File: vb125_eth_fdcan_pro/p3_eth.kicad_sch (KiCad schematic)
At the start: 43 parts, among them J4 ARJM11C7-114-BA-EW2, U2 LAN8740A, X2 50MHz

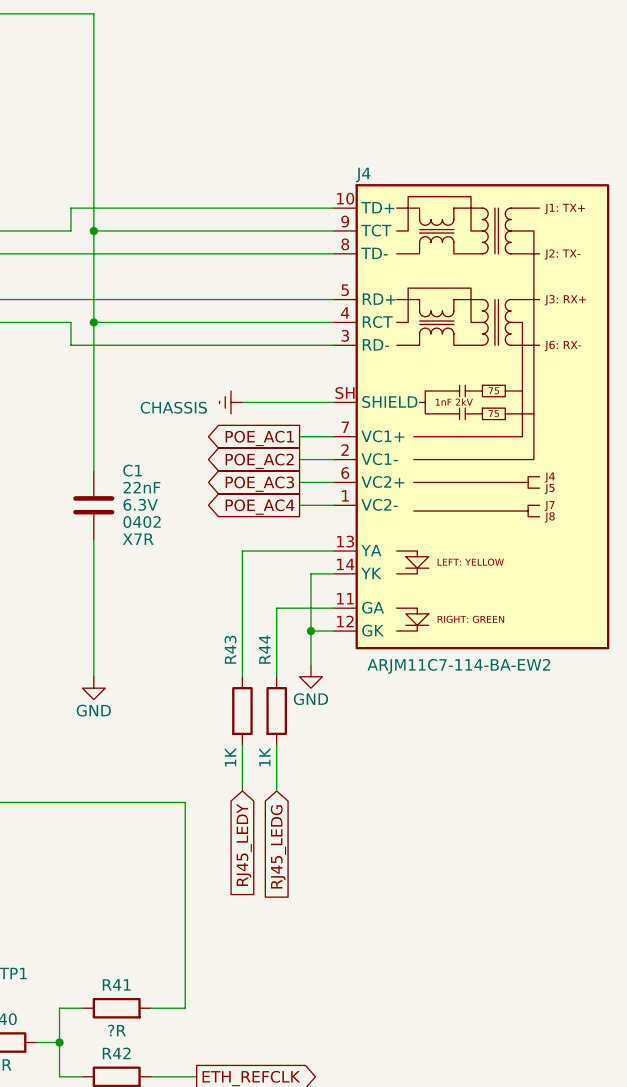
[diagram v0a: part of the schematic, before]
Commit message: Preliminary placement.
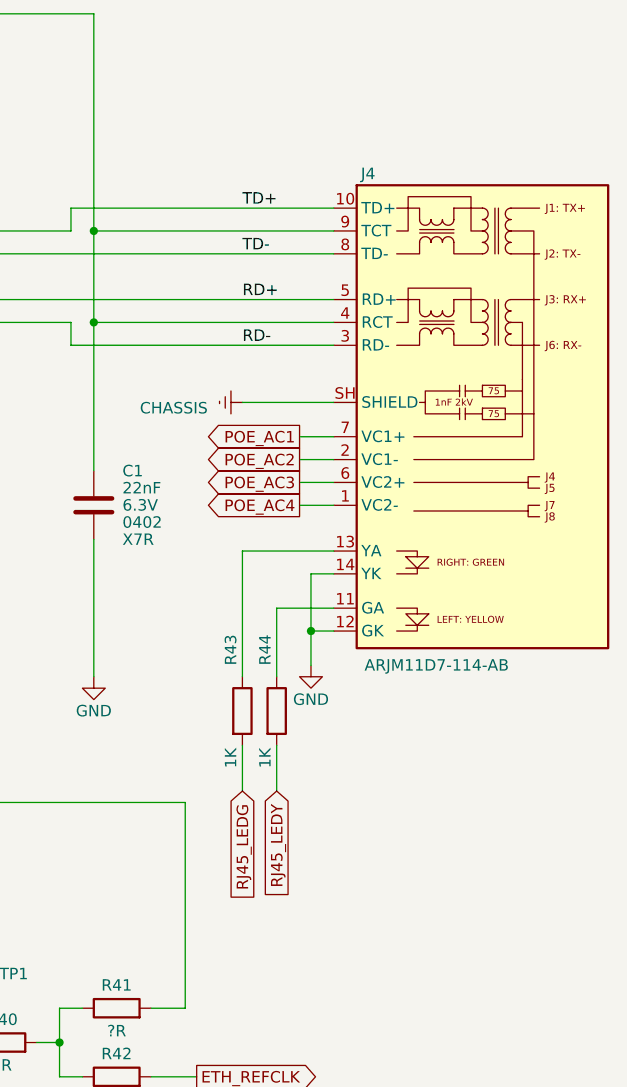
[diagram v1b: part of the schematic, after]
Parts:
- removed J4: ARJM11C7-114-BA-EW2, vhrd_connector_abracon:RJ45_Abracon_ARJM11_7POE_LED, symbol vhrd_connector_abracon:ARJM11C7-114-BA
- added J4: ARJM11D7-114-AB, vhrd_connector_abracon:ARJM11D7-114-AB-EW2, symbol vhrd_connector_abracon:ARJM11D7-114-AB
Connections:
- net +AVDD_PHY: now also J4.4 (RCT), J4.9 (TCT)
- net CHASSIS: now also J4.SH (SHIELD)
- net GND: now also J4.12 (GK), J4.14 (YK)
- net POE_AC1: now also J4.7 (VC1+)
- net POE_AC2: now also J4.2 (VC1-)
- net POE_AC3: now also J4.6 (VC2+)
- net POE_AC4: now also J4.1 (VC2-)
- net RJ45_LEDG: now also R43.2; no longer R44.2
- net RJ45_LEDY: now also R44.2; no longer R43.2
- net RD-: now reaches D1.1 (I/O_1), R35.2, U2.30 (RXN)
- net RD-: now also J4.3 (RD-)
- net TD-: now reaches D1.3 (I/O_2), R38.2, U2.28 (TXN)
- net TD-: now also J4.8 (TD-)
- net at R43.1: now also J4.13 (YA)
- net TD+: now reaches D1.4 (I/O_3), R39.2, U2.29 (TXP)
- net TD+: now also J4.10 (TD+)
- net RD+: now reaches D1.6 (I/O_4), R36.2, U2.31 (RXP)
- net RD+: now also J4.5 (RD+)
- net at R44.1: now also J4.11 (GA)
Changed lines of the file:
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@@
+    (effects (font (size 1.27 1.27)) (justify left bottom))
+  )
+  (label "RD+" (at 302.26 90.17 0) (fields_autoplaced)
     (effects (font (size 1.27 1.27)) (justify left bottom))
   )
@@
     (effects (font (size 1.27 1.27)) (justify left bottom))
   )
+  (label "TD+" (at 302.26 80.01 0) (fields_autoplaced)
+    (effects (font (size 1.27 1.27)) (justify left bottom))
+  )
   (label "PHYAD1" (at 168.91 128.27 0) (fields_autoplaced)
     (effects (font (size 1.27 1.27)) (justify left bottom))
   )
+  (label "TD-" (at 302.26 85.09 0) (fields_autoplaced)
+    (effects (font (size 1.27 1.27)) (justify left bottom))
+  )
   (label "RBIAS" (at 154.94 196.85 0) (fields_autoplaced)
     (effects (font (size 1.27 1.27)) (justify left bottom))
   )
   (label "RXD2_NU" (at 165.1 120.65 0) (fields_autoplaced)
+    (effects (font (size 1.27 1.27)) (justify left bottom))
+  )
+  (label "RD-" (at 302.26 95.25 0) (fields_autoplaced)
     (effects (font (size 1.27 1.27)) (justify left bottom))
   )
@@
     )
   )
-  (global_label "RJ45_LEDG" (shape input) (at 306.07 144.78 270) (fields_autoplaced)
+  (global_label "RJ45_LEDG" (shape input) (at 302.26 144.78 270) (fields_autoplaced)
     (effects (font (size 1.27 1.27)) (justify right))
-    (property "Intersheetrefs" "${INTERSHEET_REFS}" (at 306.07 158.0271 90)
+    (property "Intersheetrefs" "${INTERSHEET_REFS}" (at 302.26 158.0271 90)
       (effects (font (size 1.27 1.27)) (justify right) hide)
     )
   )
-  (global_label "RJ45_LEDY" (shape input) (at 302.26 144.78 270) (fields_autoplaced)
+  (global_label "RJ45_LEDY" (shape input) (at 306.07 144.78 270) (fields_autoplaced)
     (effects (font (size 1.27 1.27)) (justify right))
-    (property "Intersheetrefs" "${INTERSHEET_REFS}" (at 302.26 157.8457 90)
+    (property "Intersheetrefs" "${INTERSHEET_REFS}" (at 306.07 157.8457 90)
       (effects (font (size 1.27 1.27)) (justify right) hide)
     )
@@
     )
   )
+  (symbol (lib_id "vhrd_connector_abracon:ARJM11D7-114-AB") (at 314.96 77.47 0) (unit 1)
+    (in_bom yes) (on_board yes) (dnp no)
+    (property "Reference" "J4" (at 316.23 76.2 0)
+      (effects (font (size 1.27 1.27)))
+    )
+    (property "Value" "ARJM11D7-114-AB" (at 323.85 130.81 0)
+      (effects (font (size 1.27 1.27)))
+    )
+    (property "Footprint" "vhrd_connector_abracon:ARJM11D7-114-AB-EW2" (at 330.835 131.445 0)
+      (effects (font (size 1.27 1.27)) hide)
+    )
+    (property "Datasheet" "https://abracon.com/Magnetics/ARJM11.pdf" (at 324.485 133.35 0)
+      (effects (font (size 1.27 1.27)) hide)
+    )
+    (property "Description" "100Mbps integrated magnetics and PoE 350mA (cont)" (at 370.84 106.3625 0)
+      (effects (font (size 1.27 1.27)) hide)
+    )
+    (pin "1")
+    (pin "10")
+    (pin "11")
+    (pin "12")
+    (pin "13")
+    (pin "14")
+    (pin "2")
+    (pin "3")
+    (pin "4")
+    (pin "5")
+    (pin "6")
+    (pin "7")
+    (pin "8")
+    (pin "9")
+    (pin "SH")
+    (instances
+      (project "vb125_eth_fdcan_pro"
+        (path "/b473bccb-f14c-41d5-b473-137d3ef8ae1e/6eaf8f36-f4c1-413f-846c-b502b7be2b8c"
+          (reference "J4") (unit 1)
+        )
+      )
+    )
+  )
   (symbol (lib_id "Connector:TestPoint_Probe") (at 270.51 187.96 0) (unit 1)
     (in_bom yes) (on_board yes) (dnp no)
@@
         )
       )
-    )
-  )
-  (symbol (lib_id "vhrd_connector_abracon:ARJM11C7-114-BA") (at 314.96 77.47 0) (unit 1)
-    (in_bom yes) (on_board yes) (dnp no)
-    (property "Reference" "J4" (at 314.96 76.2 0)
-      (effects (font (size 1.27 1.27)) (justify left))
-    )
-    (property "Value" "ARJM11C7-114-BA-EW2" (at 326.39 130.81 0)
-      (effects (font (size 1.27 1.27)))
-    )
-    (property "Footprint" "vhrd_connector_abracon:RJ45_Abracon_ARJM11_7POE_LED" (at 327.66 101.6 0)
-      (effects (font (size 1.27 1.27)) hide)
-    )
-    (property "Datasheet" "https://abracon.com/Magnetics/ARJM11.pdf" (at 327.66 101.6 0)
-      (effects (font (size 1.27 1.27)) hide)
-    )
-    (property "Description" "100Mbps integrated magnetics and PoE 350mA (cont)" (at 329.565 135.255 0)
-      (effects (font (size 1.27 1.27)) hide)
-    )
-    (pin "1")
-    (pin "10")
-    (pin "11")
-    (pin "12")
-    (pin "13")
-    (pin "14")
-    (pin "2")
-    (pin "3")
-    (pin "4")
-    (pin "5")
-    (pin "6")
-    (pin "7")
-    (pin "8")
-    (pin "9")
-    (pin "SH")
-    (instances
-      (project "vb125_eth_fdcan_pro"
-        (path "/b473bccb-f14c-41d5-b473-137d3ef8ae1e/6eaf8f36-f4c1-413f-846c-b502b7be2b8c"
-          (reference "J4") (unit 1)
-        )
-      )

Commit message: Finish layout.
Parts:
- removed C1: 100nF, Capacitor_SMD:C_0402_1005Metric, symbol Device:C
- removed D1: D5V0P4UR6SO-7, vhrd_passive_tvs:D5V0P4UR6SO-7, symbol vhrd_passive_tvs:D5V0P4UR6SO-7
- added D16 (x2): RCLAMP0502BA, Package_TO_SOT_SMD:SOT-416, symbol Power_Protection:RCLAMP0502BA
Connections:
- net CHASSIS: now also D16.3 (A), D16.3 (A)
- net RD+ renamed RD_P
- net RD_P: now also D16.1 (K1)
- net RD- renamed RD_N
- net RD_N: now also D16.2 (K2)
- net TD+ renamed TD_P
- net TD_P: now also D16.1 (K1)
- net TD- renamed TD_N
- net TD_N: now also D16.2 (K2)

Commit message: Update outline.
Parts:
- X2: footprint Oscillator:Oscillator_SMD_Abracon_ASE-4Pin_3.2x2.5mm -> vhrd_crystal:Oscillator_SMD_Abracon_ASE-4Pin_3.2x2.5mm
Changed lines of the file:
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@@
       (effects (font (size 1.27 1.27)) (justify left))
     )
-    (property "Footprint" "Oscillator:Oscillator_SMD_Abracon_ASE-4Pin_3.2x2.5mm" (at 278.13 181.61 0)
+    (property "Footprint" "vhrd_crystal:Oscillator_SMD_Abracon_ASE-4Pin_3.2x2.5mm" (at 278.13 181.61 0)
       (effects (font (size 1.27 1.27)) hide)
     )
